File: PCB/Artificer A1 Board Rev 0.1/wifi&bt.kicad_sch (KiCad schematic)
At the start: 2 parts

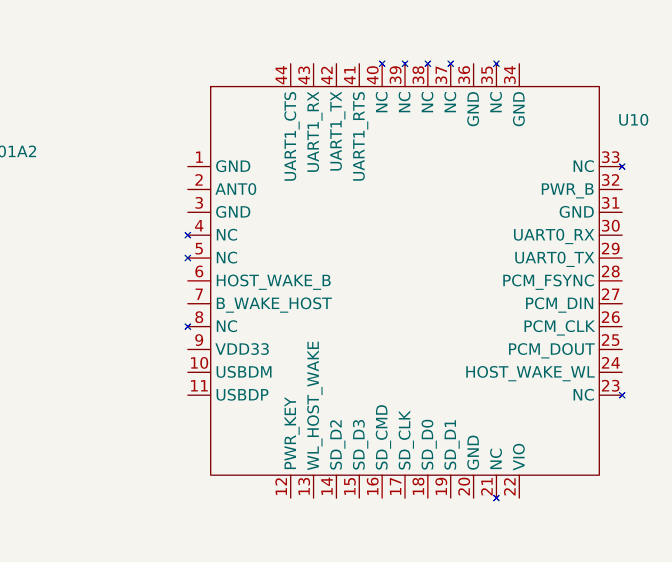
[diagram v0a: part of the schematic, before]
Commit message: schematic update
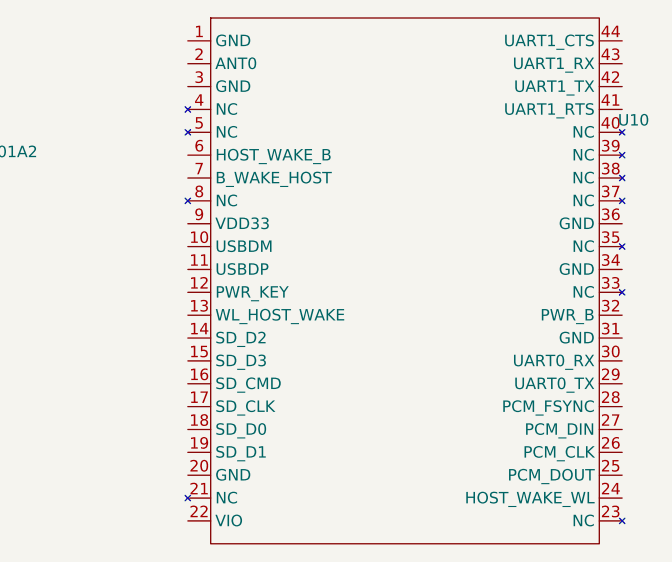
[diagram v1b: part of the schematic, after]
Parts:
- U10: footprint M8800DS2-40:M8800DS2-40 -> local_footprints:M8800DS2-40
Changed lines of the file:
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@@
 			)
 		)
-		(property "Footprint" "M8800DS2-40:M8800DS2-40"
+		(property "Footprint" "local_footprints:M8800DS2-40"
 			(at 143.256 99.568 0)
 			(effects

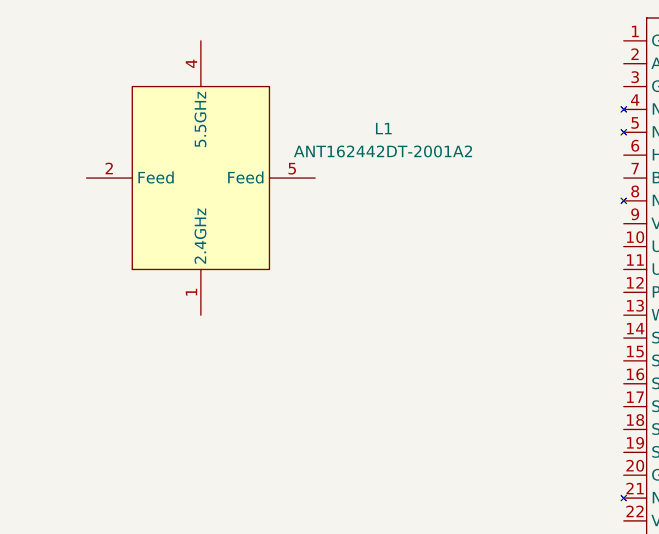
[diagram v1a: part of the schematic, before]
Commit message: localized libraries
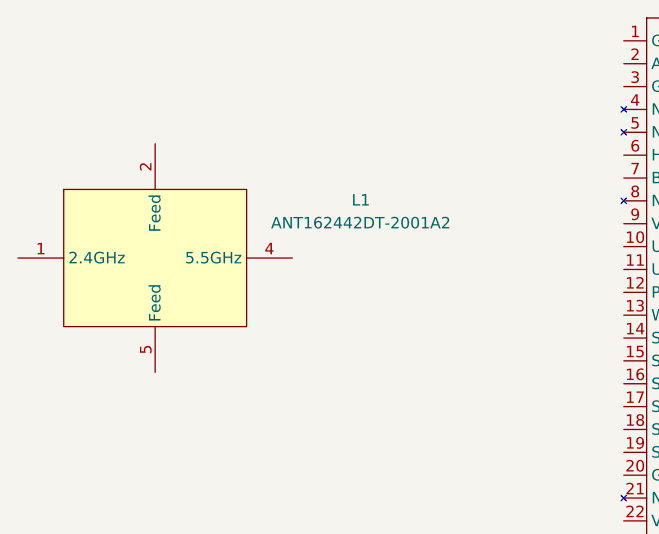
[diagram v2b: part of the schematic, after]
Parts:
- removed L1: ANT162442DT-2001A2, easyeda2kicad:ANT-SMD_6P-L1.6-W0.8-L, symbol easyeda2kicad:ANT162442DT-2001A2
- added L1: ANT162442DT-2001A2, easyeda:ANT-SMD_6P-L1.6-W0.8-L, symbol easyeda:ANT162442DT-2001A2
- U10: footprint local_footprints:M8800DS2-40 -> custom footprints:M8800DS2-40
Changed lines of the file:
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@@
+	)
+	(symbol
+		(lib_id "easyeda:ANT162442DT-2001A2")
+		(at 69.85 101.6 0)
+		(unit 1)
+		(exclude_from_sim no)
+		(in_bom yes)
+		(on_board yes)
+		(dnp no)
+		(fields_autoplaced yes)
+		(property "Reference" "L1"
+			(at 92.71 95.1798 0)
+			(effects
+				(font
+					(size 1.27 1.27)
+				)
+			)
+		)
+		(property "Value" "ANT162442DT-2001A2"
+			(at 92.71 97.7198 0)
+			(effects
+				(font
+					(size 1.27 1.27)
+				)
+			)
+		)
+		(property "Footprint" "easyeda:ANT-SMD_6P-L1.6-W0.8-L"
+			(at 69.85 121.92 0)
+			(effects
+				(font
+					(size 1.27 1.27)
+				)
+				(hide yes)
+			)
+		)
+		(property "Datasheet" "https://lcsc.com/product-detail/Pre-ordered-Products_TDK_ANT162442DT-2001A2_TDK-ANT162442DT-2001A2_C531339.html"
+			(at 69.85 124.46 0)
+			(effects
+				(font
+					(size 1.27 1.27)
+				)
+				(hide yes)
+			)
+		)
+		(property "Description" ""
+			(at 69.85 101.6 0)
+			(effects
+				(font
+					(size 1.27 1.27)
+				)
+				(hide yes)
+			)
+		)
+		(property "LCSC Part" "C531339"
+			(at 69.85 127 0)
+			(effects
+				(font
+					(size 1.27 1.27)
+				)
+				(hide yes)
+			)
+		)
+		(pin "2"
+		)
+		(pin "1"
+		)
+		(pin "5"
+		)
+		(pin "4"
+		)
+		(instances
+			(project ""
+				(path "/7c37bdb5-94b0-4567-b5ec-a879db855389/bb518e39-315f-4fac-931f-ad14a14e5ca9"
+					(reference "L1")
+					(unit 1)
+				)
+			)
+		)
 	)
 	(symbol
@@
 			)
 		)
-		(property "Footprint" "local_footprints:M8800DS2-40"
+		(property "Footprint" "custom footprints:M8800DS2-40"
 			(at 143.256 99.568 0)
 			(effects
@@
 			)
 		)
-		(property "Datasheet" "part datasheets/AIC8800D80_DataSheet_v0.1.pdf"
+		(property "Datasheet" "libs/_datasheets/AIC8800D80_DataSheet_v0.1.pdf"
 			(at 146.05 104.14 0)
 			(effects
@@
 					(unit 1)
 				)
-			)
-		)
-	)
-	(symbol
-		(lib_id "easyeda2kicad:ANT162442DT-2001A2")
-		(at 74.93 92.71 90)
-		(unit 1)
-		(exclude_from_sim no)
-		(in_bom yes)
-		(on_board yes)
-		(dnp no)
-		(fields_autoplaced yes)
-		(property "Reference" "L1"
-			(at 95.25 87.2646 90)
-			(effects
-				(font
-					(size 1.27 1.27)
-				)
-			)
-		)
-		(property "Value" "ANT162442DT-2001A2"
-			(at 95.25 89.8046 90)
-			(effects
-				(font
-					(size 1.27 1.27)
-				)
-			)
-		)
-		(property "Footprint" "easyeda2kicad:ANT-SMD_6P-L1.6-W0.8-L"
-			(at 95.25 92.71 0)
-			(effects
-				(font
-					(size 1.27 1.27)
-				)
-				(hide yes)
-			)
-		)
-		(property "Datasheet" "https://lcsc.com/product-detail/Pre-ordered-Products_TDK_ANT162442DT-2001A2_TDK-ANT162442DT-2001A2_C531339.html"
-			(at 97.79 92.71 0)
-			(effects
-				(font
-					(size 1.27 1.27)
-				)
-				(hide yes)
-			)
-		)
-		(property "Description" ""
-			(at 74.93 92.71 0)
-			(effects
-				(font
-					(size 1.27 1.27)
-				)
-				(hide yes)
-			)
-		)
-		(property "LCSC Part" "C531339"
-			(at 100.33 92.71 0)
-			(effects
-				(font
-					(size 1.27 1.27)
-				)
-				(hide yes)
-			)
-		)
-		(pin "1"
-		)
-		(pin "2"
-		)
-		(pin "5"
-		)
-		(pin "4"
-		)
-		(instances
-			(project ""
-				(path "/7c37bdb5-94b0-4567-b5ec-a879db855389/bb518e39-315f-4fac-931f-ad14a14e5ca9"
-					(reference "L1")
-					(unit 1)
-				)

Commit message: added a few accessories
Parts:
- added JP1: U.FL-R-SMT-1(80), easyeda:RF-SMD_FRF05002-JSS103M, symbol easyeda:U.FL-R-SMT-1(80)
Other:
- note added: "This is a 1 Inner pin IPEX connector for connecting an eternal antenna if I learn how to implement both"
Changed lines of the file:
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@@
 		(company "Matthew Spotten")
+	)
+	(text "This is a 1 Inner pin IPEX connector for connecting an eternal antenna if I learn how to implement both"
+		(exclude_from_sim no)
+		(at 69.85 159.258 0)
+		(effects
+			(font
+				(size 1.27 1.27)
+			)
+		)
 	)
 	(symbol
@@
 					(unit 1)
 				)
+			)
+		)
+	)
+	(symbol
+		(lib_id "easyeda:U.FL-R-SMT-1(80)")
+		(at 69.85 148.59 0)
+		(unit 1)
+		(exclude_from_sim no)
+		(in_bom yes)
+		(on_board yes)
+		(dnp no)
+		(fields_autoplaced yes)
+		(property "Reference" "JP1"
+			(at 69.85 138.43 0)
+			(effects
+				(font
+					(size 1.27 1.27)
+				)
+			)
+		)
+		(property "Value" "U.FL-R-SMT-1(80)"
+			(at 69.85 140.97 0)
+			(effects
+				(font
+					(size 1.27 1.27)
+				)
+			)
+		)
+		(property "Footprint" "easyeda:RF-SMD_FRF05002-JSS103M"
+			(at 69.85 161.29 0)
+			(effects
+				(font
+					(size 1.27 1.27)
+				)
+				(hide yes)
+			)
+		)
+		(property "Datasheet" "https://lcsc.com/product-detail/Connectors_HRS_U-FL-R-SMT-1-80_3310472280-IPE-XBoard-end-IPXConnector-SMD_C88374.html"
+			(at 69.85 163.83 0)
+			(effects
+				(font
+					(size 1.27 1.27)
+				)
+				(hide yes)
+			)
+		)
+		(property "Description" ""
+			(at 69.85 148.59 0)
+			(effects
+				(font
+					(size 1.27 1.27)
+				)
+				(hide yes)
+			)
+		)
+		(property "LCSC Part" "C88374"
+			(at 69.85 166.37 0)
+			(effects
+				(font
+					(size 1.27 1.27)
+				)
+				(hide yes)
+			)
+		)
+		(pin "1"
+		)
+		(pin "3"
+		)
+		(pin "2"
+		)
+		(instances
+			(project ""
+				(path "/7c37bdb5-94b0-4567-b5ec-a879db855389/bb518e39-315f-4fac-931f-ad14a14e5ca9"
+					(reference "JP1")
+					(unit 1)
+				)
